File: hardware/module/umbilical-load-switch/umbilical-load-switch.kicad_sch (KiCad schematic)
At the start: 11 parts

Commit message: WIP module schematics: footprints, bought-part fields, and the two board projects (module-main, module-jack)
Recovered from a container restart; not yet exported or checked.

Co-Authored-By: Claude Opus 5.5 <noreply@anthropic.com>
Claude-Session: https://claude.ai/code/session_01LmB4muFXnoLprWX4JzuJ5A
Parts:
- C-DECOUPLE-LOADSW: footprint (none) -> Capacitor_SMD:C_0805_2012Metric; Assembly (none) -> machine; LCSC (none) -> C49678; MPN (none) -> CC0805KRX7R9BB104; Manufacturer (none) -> YAGEO
- C-GATE-LOADSW: footprint (none) -> Capacitor_SMD:C_1206_3216Metric; Assembly (none) -> machine; LCSC (none) -> C97947; MPN (none) -> GRM31C5C1H823JA01L; Manufacturer (none) -> Murata
- C-TIMER-LOADSW: footprint (none) -> Capacitor_SMD:C_1210_3225Metric; Assembly (none) -> machine; LCSC (none) -> C77100; MPN (none) -> GRM32DR71E106KA12L; Manufacturer (none) -> Murata
- Q-LOADSW: footprint (none) -> Package_TO_SOT_SMD:TO-252-2; Assembly (none) -> hand
- R-FB-HI: footprint (none) -> Resistor_SMD:R_0805_2012Metric; Assembly (none) -> machine; LCSC (none) -> C2849191; MPN (none) -> PTFR0805B35K7P9; Manufacturer (none) -> RESI
- R-FB-LO: footprint (none) -> Resistor_SMD:R_0805_2012Metric; Assembly (none) -> machine; LCSC (none) -> C865574; MPN (none) -> RT0805BRD075K11L; Manufacturer (none) -> YAGEO
- R-GATE-COMP: footprint (none) -> Resistor_SMD:R_0805_2012Metric; Assembly (none) -> machine; LCSC (none) -> C17513; MPN (none) -> 0805W8F1001T5E; Manufacturer (none) -> UNI-ROYAL(Uniroyal Elec)
- R-GATE-SER: footprint (none) -> Resistor_SMD:R_0805_2012Metric; Assembly (none) -> machine; LCSC (none) -> C17415; MPN (none) -> 0805W8F100JT5E; Manufacturer (none) -> UNI-ROYAL(Uniroyal Elec)
- R-ILIM: footprint (none) -> Resistor_SMD:R_1206_3216Metric; Assembly (none) -> hand
- SW-POWER: footprint (none) -> Connector_Wire:SolderWire-0.25sqmm_1x02_P4.2mm_D0.65mm_OD1.7mm; Assembly (none) -> hand; MPN (none) -> M2011SD4G01; Manufacturer (none) -> NKK Switches
- U-LOADSW: footprint (none) -> Package_SO:SOIC-8_3.9x4.9mm_P1.27mm; Assembly (none) -> hand; LCSC (none) -> C664550; MPN (none) -> LT1641-1CS8#PBF; Manufacturer (none) -> Analog Devices

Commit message: Module load switch: ON divider drawn, pass FET and sense resistor chosen, I grade, gate clamp
SW-POWER now sits in the top leg of the LT1641 ON divider (R-ON-HI 68k /
R-ON-LO 10k, C-ON-LOADSW 100nF): on at 10.24 V, off at 9.62 V typ. Both
toggle lugs wire to the main board (ADR 0024 open row closed).
Q-LOADSW = Nexperia PSMN2R0-30YLE, chosen on its SOA at 12 V (banked, R31);
D-GATE-CLAMP 15 V zener as the LT1641 datasheet requires below 24 V.
R-ILIM fixed at 50 mohm (RALEC LR1206, banked): the hot-plug finishes inside
the fault time at the low corner of every threshold. U-LOADSW is the I grade.
Corrects the page's '~4 W peak at V_out ~4 V' (it is 7.5-8.8 W there).

Co-Authored-By: Claude Opus 5.5 <noreply@anthropic.com>
Claude-Session: https://claude.ai/code/session_01LmB4muFXnoLprWX4JzuJ5A
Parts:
- added C-ON-LOADSW: 100nF, Capacitor_SMD:C_0805_2012Metric, symbol Device:C
- added D-GATE-CLAMP: 15V, Diode_SMD:D_SOD-123, symbol Device:D_Zener
- added R-ON-HI: 68k 1%, Resistor_SMD:R_0805_2012Metric, symbol Device:R
- added R-ON-LO: 10k 1%, Resistor_SMD:R_0805_2012Metric, symbol Device:R
- Q-LOADSW: value (none) -> PSMN2R0-30YLE; footprint Package_TO_SOT_SMD:TO-252-2 -> Package_TO_SOT_SMD:LFPAK56; symbol Transistor_FET:Q_NMOS_GDS -> Transistor_FET:PSMN5R2-60YL; Assembly hand -> machine; LCSC (none) -> C553247; MPN (none) -> PSMN2R0-30YLE,115; Manufacturer (none) -> Nexperia; Note Pass FET, high side. Its drain is always at 12 V, which is 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 -> Pass FET, high side, chosen on its SOA at V_DS = 12 V (umbi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; Pins D=2(D) G=1(G) S=3(S) -> D=5(D) G=4(G) S=1(S) S2=2(S) S3=3(S); Pins_source the part is not chosen (Q-LOADSW row); 1 G, 2 D (the tab), 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 -> datasheets/discrete-and-power/NEXPERIA-PSMN2R0-30YLE.pdf p.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
- R-ILIM: value (none) -> 50m 1% 1W; Assembly hand -> machine; LCSC (none) -> C154645; MPN (none) -> LR1206-21R050F4; Manufacturer (none) -> RALEC; Note Sets the limit with V_SENSETRIP, which is 39/47/55 mV - so the limit has a spread whatever this resistor is -> Sets the limit with V_SENSETRIP, which is 39/47/55 mV - so the limit has a spread whatever this resistor is: 0.78/0.94/1.10 A at 50 mohm. Kelvin-connect SENSE and VCC to its pads (164112fc p.10, Layout Considerations)
- SW-POWER: Note THE SWITCH IS THIS CIRCUIT'S PART. module/panel owns only the shaped hole and says so. Its other terminal waits on the UVLO divider - see ON_DIVIDER -> THE SWITCH IS THIS CIRCUIT'S PART. module/panel owns only the shaped hole and says so. COM on ON, NO on ON_SW: the switch sits between R-ON-HI and the ON pin, so closing it (lever right, ADR 0024 point 12) completes the UVLO divider and opening it lets R-ON-LO pull ON low. Both lugs wire to this board
- U-LOADSW: value LT1641-1CS8 -> LT1641-1IS8; LCSC C664550 -> C664552; MPN LT1641-1CS8#PBF -> LT1641-1IS8#PBF
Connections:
- net BUS_POS12_RAW: now also R-ON-HI.1
- net GATE_NODE: now also Q-LOADSW.4 (G), D-GATE-CLAMP.1 (K); no longer Q-LOADSW.1 (G)
- net ON: now also C-ON-LOADSW.1, R-ON-LO.1
- net PWR_GND: now also C-ON-LOADSW.2, R-ON-LO.2
- net SENSE_NODE: now also Q-LOADSW.5 (D); no longer Q-LOADSW.2 (D)
- net UMBILICAL_POS12: now also Q-LOADSW.1 (S), Q-LOADSW.2 (S), D-GATE-CLAMP.2 (A)
- net ON_SW: now reaches SW-POWER.2 (B)
- net ON_SW: now also R-ON-HI.2
- no-connect marks 2 -> 1
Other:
- note added: "AUTHORITATIVE for connectivity. The part notes are on each part's Note field. THIS CIRCUIT IS DRAWN ON ANOTHER PAGE. The load switch sits inside power-entry.md's entry drawing, deliberately, because that is one board and one drawing; this page carries only the gate-network detail. So the labels that describe these parts are on a page whose netlist does not own them - which is why tools/check-netl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"
- note removed: "FROM THE HAND-WRITTEN NETLIST THIS SHEET REPLACES (verbatim; the part notes are on each part's Note field): A LONE NO-CONNECT PIN'S NET IS NAMED AFTER THE PIN (the export names it so, whatever label it carries), so the one-pin nets the text below names are, on this sheet: ON_DIVIDER is NO. AUTHORITATIVE for connectivity. THIS CIRCUIT IS DRAWN ON ANOTHER PAGE. The load switch sits inside power-ent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"

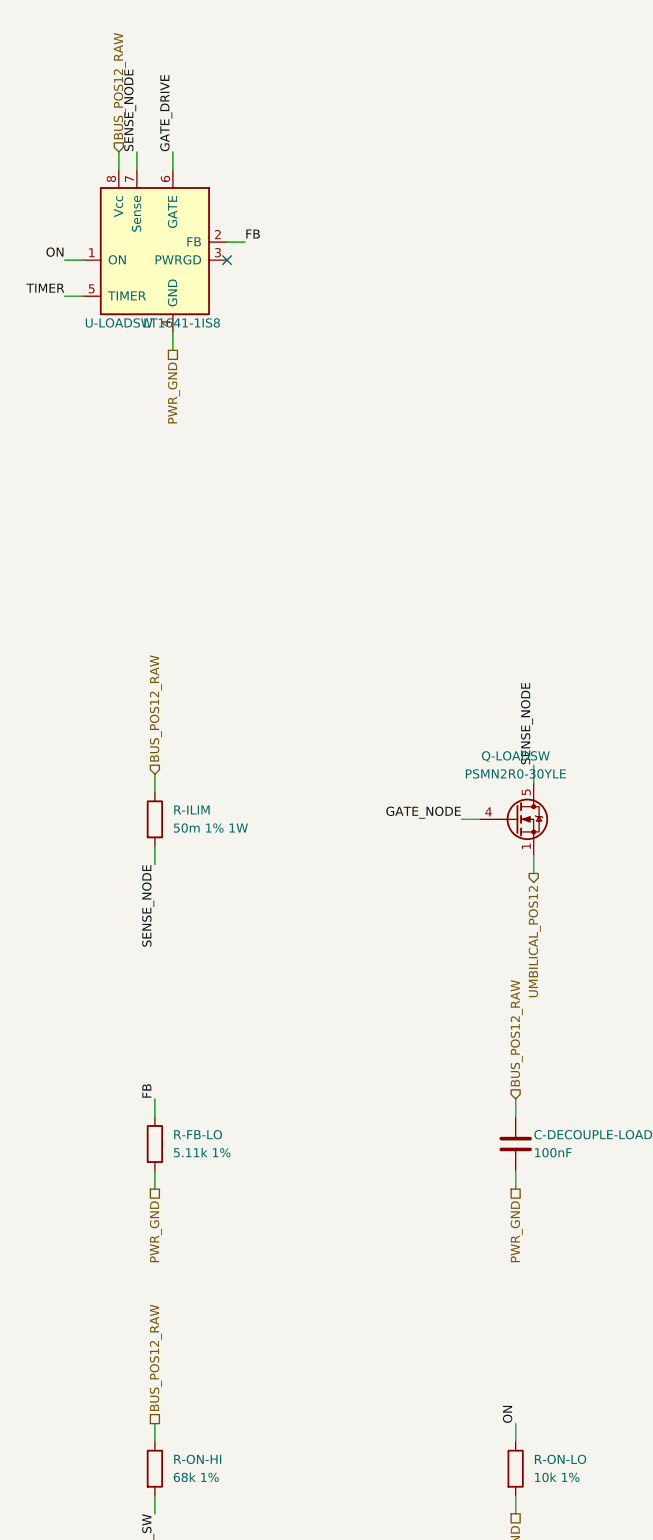
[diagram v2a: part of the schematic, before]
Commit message: WIP module power entry: rail PTCs, the instrument's isolated supply (U-ISO), ground split
Sheets, exports, BOM rows, banked datasheets (manifest fragment to follow).
The page drawing, ADR 0027, figures and sims are the next commits.

Co-Authored-By: Claude Opus 5.5 <noreply@anthropic.com>
Claude-Session: https://claude.ai/code/session_01LmB4muFXnoLprWX4JzuJ5A
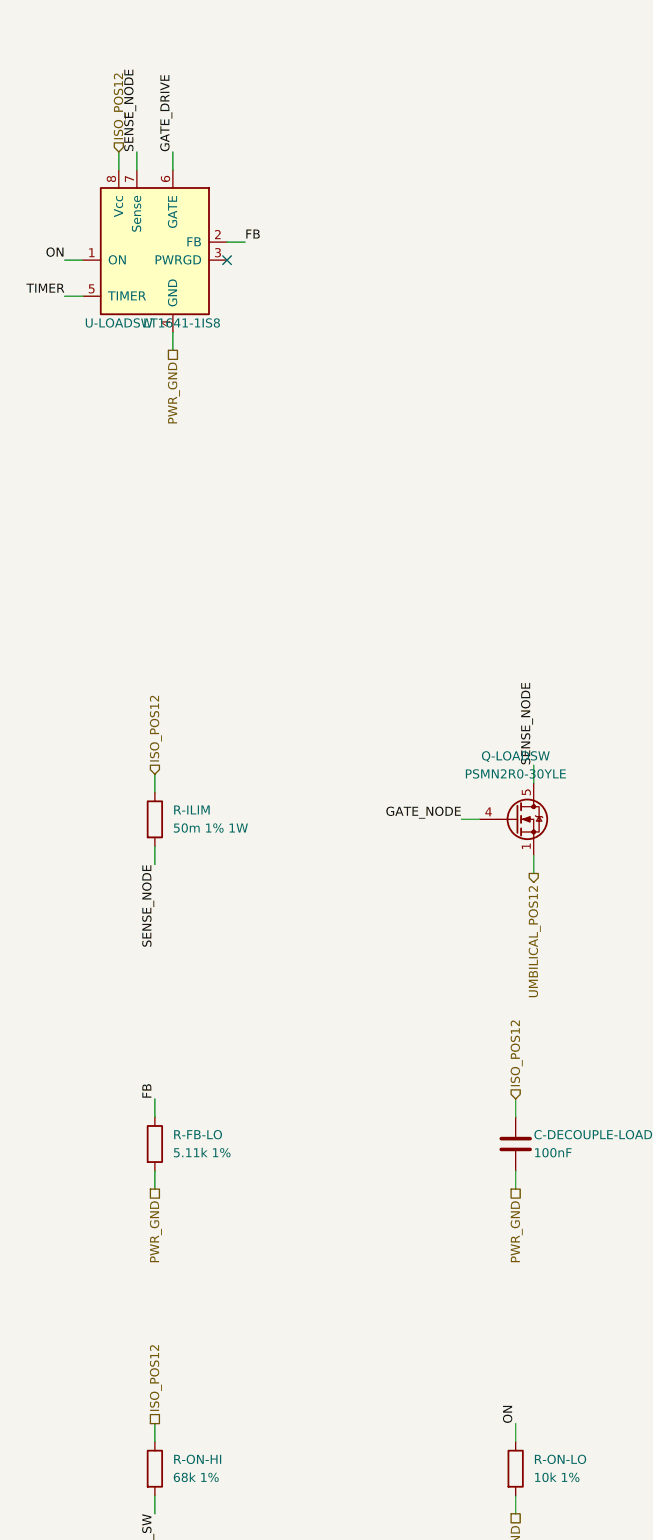
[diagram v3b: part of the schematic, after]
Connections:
- net BUS_POS12_RAW renamed ISO_POS12
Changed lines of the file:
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@@
   )
   (wire (pts (xy 35.56 50.8) (xy 35.56 48.26)) (stroke (width 0) (type default)))
-  (hierarchical_label "BUS_POS12_RAW" (shape input) (at 35.56 48.26 90) (effects (font (size 1.27 1.27)) (justify left))
+  (hierarchical_label "ISO_POS12" (shape input) (at 35.56 48.26 90) (effects (font (size 1.27 1.27)) (justify left))
     (property "Dir" "in" (at 35.56 48.26 0) (effects (font (size 1.27 1.27)) hide))
     (property "From" "module/power-entry" (at 35.56 48.26 0) (effects (font (size 1.27 1.27)) hide)))
   (wire (pts (xy 40.64 138.43) (xy 40.64 135.89)) (stroke (width 0) (type default)))
-  (hierarchical_label "BUS_POS12_RAW" (shape input) (at 40.64 135.89 90) (effects (font (size 1.27 1.27)) (justify left))
+  (hierarchical_label "ISO_POS12" (shape input) (at 40.64 135.89 90) (effects (font (size 1.27 1.27)) (justify left))
     (property "Dir" "in" (at 40.64 135.89 0) (effects (font (size 1.27 1.27)) hide))
     (property "From" "module/power-entry" (at 40.64 135.89 0) (effects (font (size 1.27 1.27)) hide)))
   (wire (pts (xy 91.44 184.15) (xy 91.44 181.61)) (stroke (width 0) (type default)))
-  (hierarchical_label "BUS_POS12_RAW" (shape input) (at 91.44 181.61 90) (effects (font (size 1.27 1.27)) (justify left))
+  (hierarchical_label "ISO_POS12" (shape input) (at 91.44 181.61 90) (effects (font (size 1.27 1.27)) (justify left))
     (property "Dir" "in" (at 91.44 181.61 0) (effects (font (size 1.27 1.27)) hide))
     (property "From" "module/power-entry" (at 91.44 181.61 0) (effects (font (size 1.27 1.27)) hide)))
@@
   )
   (wire (pts (xy 40.64 229.87) (xy 40.64 227.33)) (stroke (width 0) (type default)))
-  (hierarchical_label "BUS_POS12_RAW" (shape passive) (at 40.64 227.33 90) (effects (font (size 1.27 1.27)) (justify left))
+  (hierarchical_label "ISO_POS12" (shape passive) (at 40.64 227.33 90) (effects (font (size 1.27 1.27)) (justify left))
     (property "Dir" "in" (at 40.64 227.33 0) (effects (font (size 1.27 1.27)) hide))
     (property "From" "module/power-entry" (at 40.64 227.33 0) (effects (font (size 1.27 1.27)) hide)))

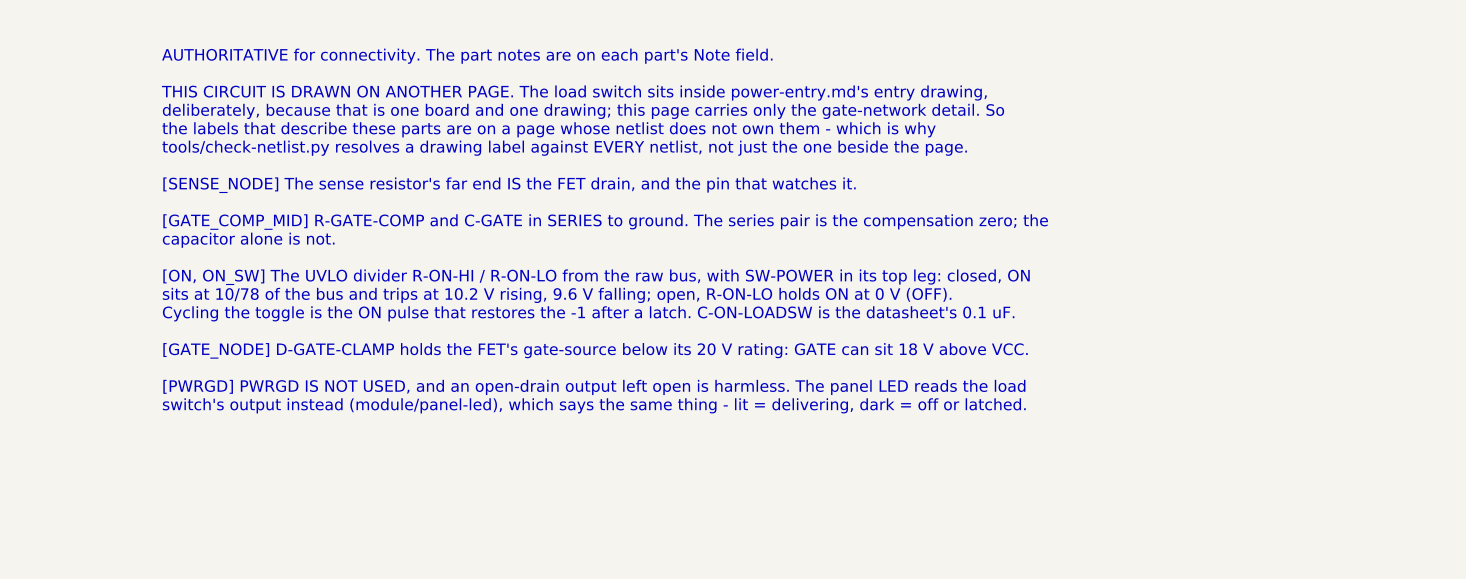
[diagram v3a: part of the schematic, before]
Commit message: ADR 0027 follow-through: load switch page and sheet on ISO_POS12, ADR 0004/0005 amendments, sims re-run, renders
The load switch page states its new supply and the margins it gains (ON
turn-on 0.94 V below U-ISO's floor, was 0.7 V below the bus's); sheet notes
and text follow; the power-entry sheet no longer declares foreign parts its
drawing stopped showing. ADR 0004 and 0005 carry dated amendments pointing
at ADR 0027; pitch-stage.md's exclusion reads as removed. Sim READMEs record
the ground-shift decks and the LM317L model's non-convergence at the fuse's
post-trip 6 ohm. All gates pass; sims re-run on the final netlists.

Co-Authored-By: Claude Opus 5.5 <noreply@anthropic.com>
Claude-Session: https://claude.ai/code/session_01LmB4muFXnoLprWX4JzuJ5A
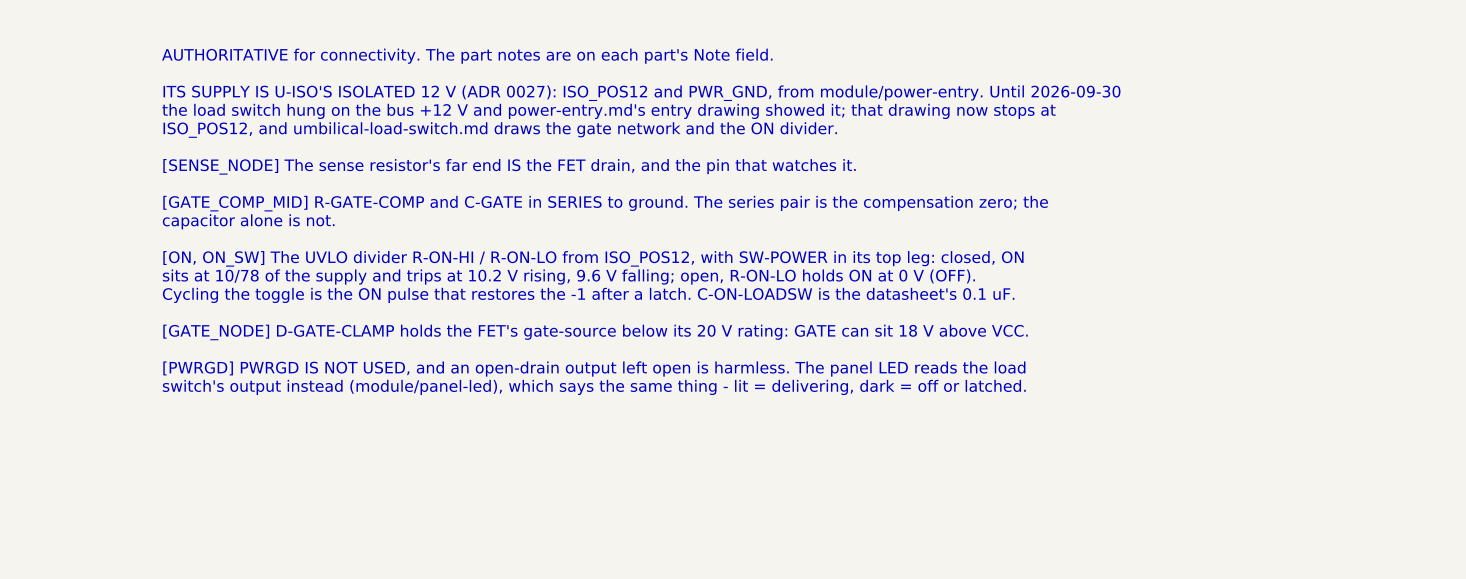
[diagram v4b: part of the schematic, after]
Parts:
- R-ON-HI: Note Top of the ON (UVLO) divider, from the raw bus through the 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 -> Top of the ON (UVLO) divider, from ISO_POS12 - U-ISO's isol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
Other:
- note added: "AUTHORITATIVE for connectivity. The part notes are on each part's Note field. ITS SUPPLY IS U-ISO'S ISOLATED 12 V (ADR 0027): ISO_POS12 and PWR_GND, from module/power-entry. Until 2026-09-30 the load switch hung on the bus +12 V and power-entry.md's entry drawing showed it; that drawing now stops at ISO_POS12, and umbilical-load-switch.md draws the gate network and the ON divider. [SENSE_NODE] Th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"
- note removed: "AUTHORITATIVE for connectivity. The part notes are on each part's Note field. THIS CIRCUIT IS DRAWN ON ANOTHER PAGE. The load switch sits inside power-entry.md's entry drawing, deliberately, because that is one board and one drawing; this page carries only the gate-network detail. So the labels that describe these parts are on a page whose netlist does not own them - which is why tools/check-netl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"
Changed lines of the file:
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@@
     (property "From" "module/power-entry" (at 91.44 194.31 0) (effects (font (size 1.27 1.27)) hide)))
   (no_connect (at 50.8 63.5))
-  (text "AUTHORITATIVE for connectivity. The part notes are on each part's Note field.\n\nTHIS CIRCUIT IS DRAWN ON ANOTHER PAGE. The load switch sits inside power-entry.md's entry drawing,\ndeliberately, because that is one board and one drawing; this page carries only the gate-network detail. So\nthe labels that describe these parts are on a page whose netlist does not own them - which is why\ntools/check-netlist.py resolves a drawing label against EVERY netlist, not just the one beside the page.\n\n[SENSE_NODE] The sense resistor's far end IS the FET drain, and the pin that watches it.\n\n[GATE_COMP_MID] R-GATE-COMP and C-GATE in SERIES to ground. The series pair is the compensation zero; the\ncapacitor alone is not.\n\n[ON, ON_SW] The UVLO divider R-ON-HI / R-ON-LO from the raw bus, with SW-POWER in its top leg: closed, ON\nsits at 10/78 of the bus and trips at 10.2 V rising, 9.6 V falling; open, R-ON-LO holds ON at 0 V (OFF).\nCycling the toggle is the ON pulse that restores the -1 after a latch. C-ON-LOADSW is the datasheet's 0.1 uF.\n\n[GATE_NODE] D-GATE-CLAMP holds the FET's gate-source below its 20 V rating: GATE can sit 18 V above VCC.\n\n[PWRGD] PWRGD IS NOT USED, and an open-drain output left open is harmless. The panel LED reads the load\nswitch's output instead (module/panel-led), which says the same thing - lit = delivering, dark = off or latched." (at 408.94 38.099999999999994 0) (effects (font (size 1.27 1.27)) (justify left top)))
+  (text "AUTHORITATIVE for connectivity. The part notes are on each part's Note field.\n\nITS SUPPLY IS U-ISO'S ISOLATED 12 V (ADR 0027): ISO_POS12 and PWR_GND, from module/power-entry. Until 2026-09-30\nthe load switch hung on the bus +12 V and power-entry.md's entry drawing showed it; that drawing now stops at\nISO_POS12, and umbilical-load-switch.md draws the gate network and the ON divider.\n\n[SENSE_NODE] The sense resistor's far end IS the FET drain, and the pin that watches it.\n\n[GATE_COMP_MID] R-GATE-COMP and C-GATE in SERIES to ground. The series pair is the compensation zero; the\ncapacitor alone is not.\n\n[ON, ON_SW] The UVLO divider R-ON-HI / R-ON-LO from ISO_POS12, with SW-POWER in its top leg: closed, ON\nsits at 10/78 of the supply and trips at 10.2 V rising, 9.6 V falling; open, R-ON-LO holds ON at 0 V (OFF).\nCycling the toggle is the ON pulse that restores the -1 after a latch. C-ON-LOADSW is the datasheet's 0.1 uF.\n\n[GATE_NODE] D-GATE-CLAMP holds the FET's gate-source below its 20 V rating: GATE can sit 18 V above VCC.\n\n[PWRGD] PWRGD IS NOT USED, and an open-drain output left open is harmless. The panel LED reads the load\nswitch's output instead (module/panel-led), which says the same thing - lit = delivering, dark = off or latched." (at 408.94 38.099999999999994 0) (effects (font (size 1.27 1.27)) (justify left top)))
   (wire (pts (xy 147.32 187.96) (xy 149.86 187.96)) (stroke (width 0) (type default)))
   (label "ON_SW" (at 149.86 187.96 0) (fields_autoplaced) (effects (font (size 1.27 1.27)) (justify left bottom)))
@@
     (property "Row" "R-ON-HI" (at 40.64 233.68 0) (effects (font (size 1.27 1.27)) hide))
     (property "Pins" "1=1 2=2" (at 40.64 233.68 0) (effects (font (size 1.27 1.27)) hide))
-    (property "Note" "Top of the ON (UVLO) divider, from the raw bus through the toggle. With R-ON-LO: ON at 10.2 V rising, 9.6 V falling" (at 40.64 233.68 0) (effects (font (size 1.27 1.27)) hide))
+    (property "Note" "Top of the ON (UVLO) divider, from ISO_POS12 - U-ISO's isolated 12 V since ADR 0027 - through the toggle. With R-ON-LO: ON at 10.2 V rising, 9.6 V falling" (at 40.64 233.68 0) (effects (font (size 1.27 1.27)) hide))
     (property "Manufacturer" "UNI-ROYAL(Uniroyal Elec)" (at 40.64 233.68 0) (effects (font (size 1.27 1.27)) hide))
     (property "MPN" "0805W8F6802T5E" (at 40.64 233.68 0) (effects (font (size 1.27 1.27)) hide))
